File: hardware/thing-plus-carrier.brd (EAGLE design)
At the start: 160 x 100 mm, 6 parts, among them J1 THING_PLUS, U1 OKI-78SR-5/1.5-W36H-C

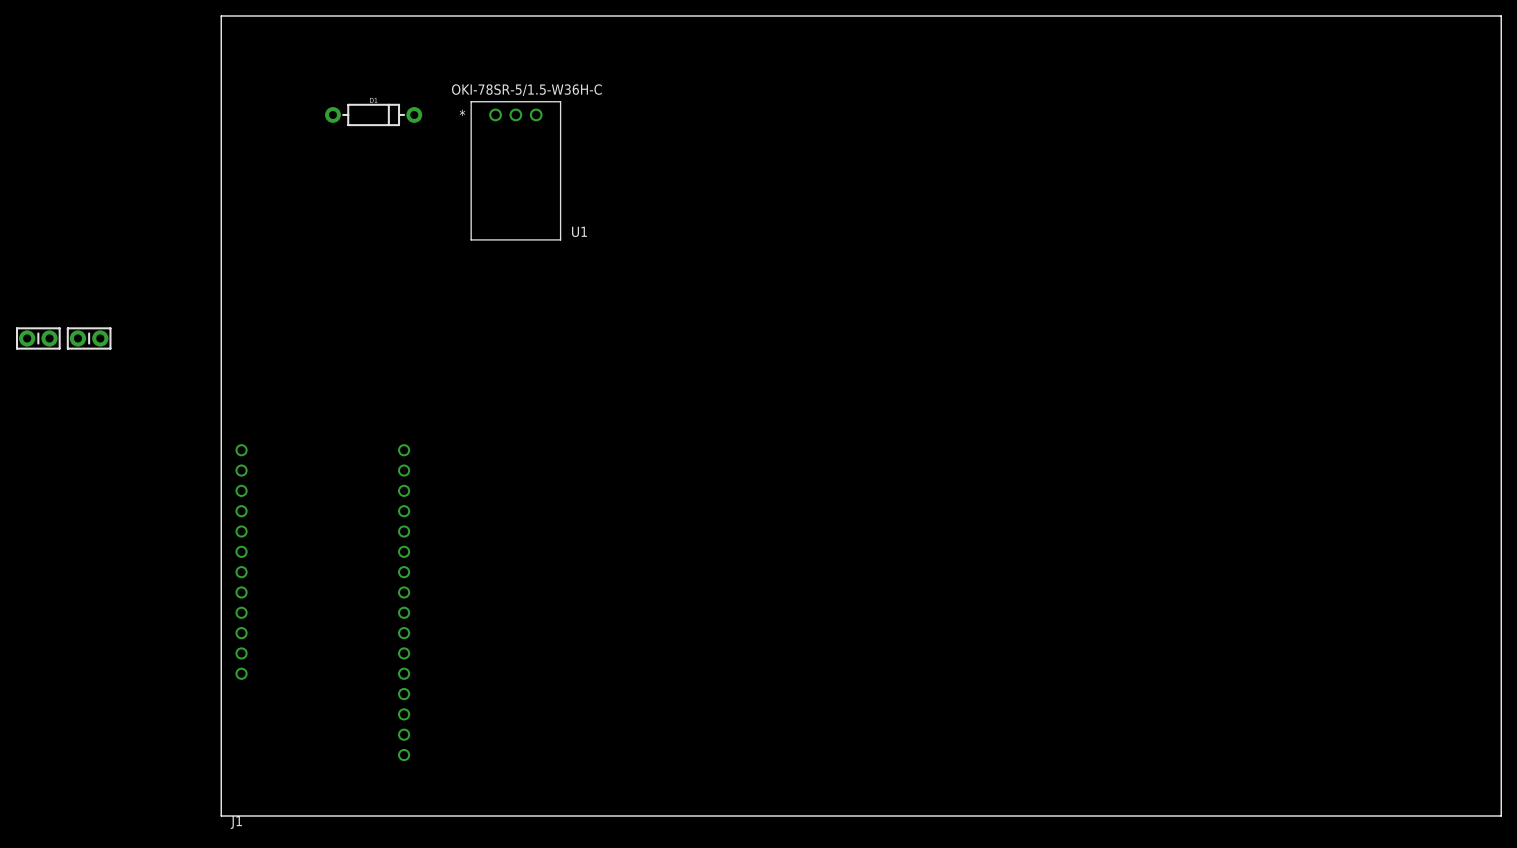
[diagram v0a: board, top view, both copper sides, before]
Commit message: laying out featherwing schematic
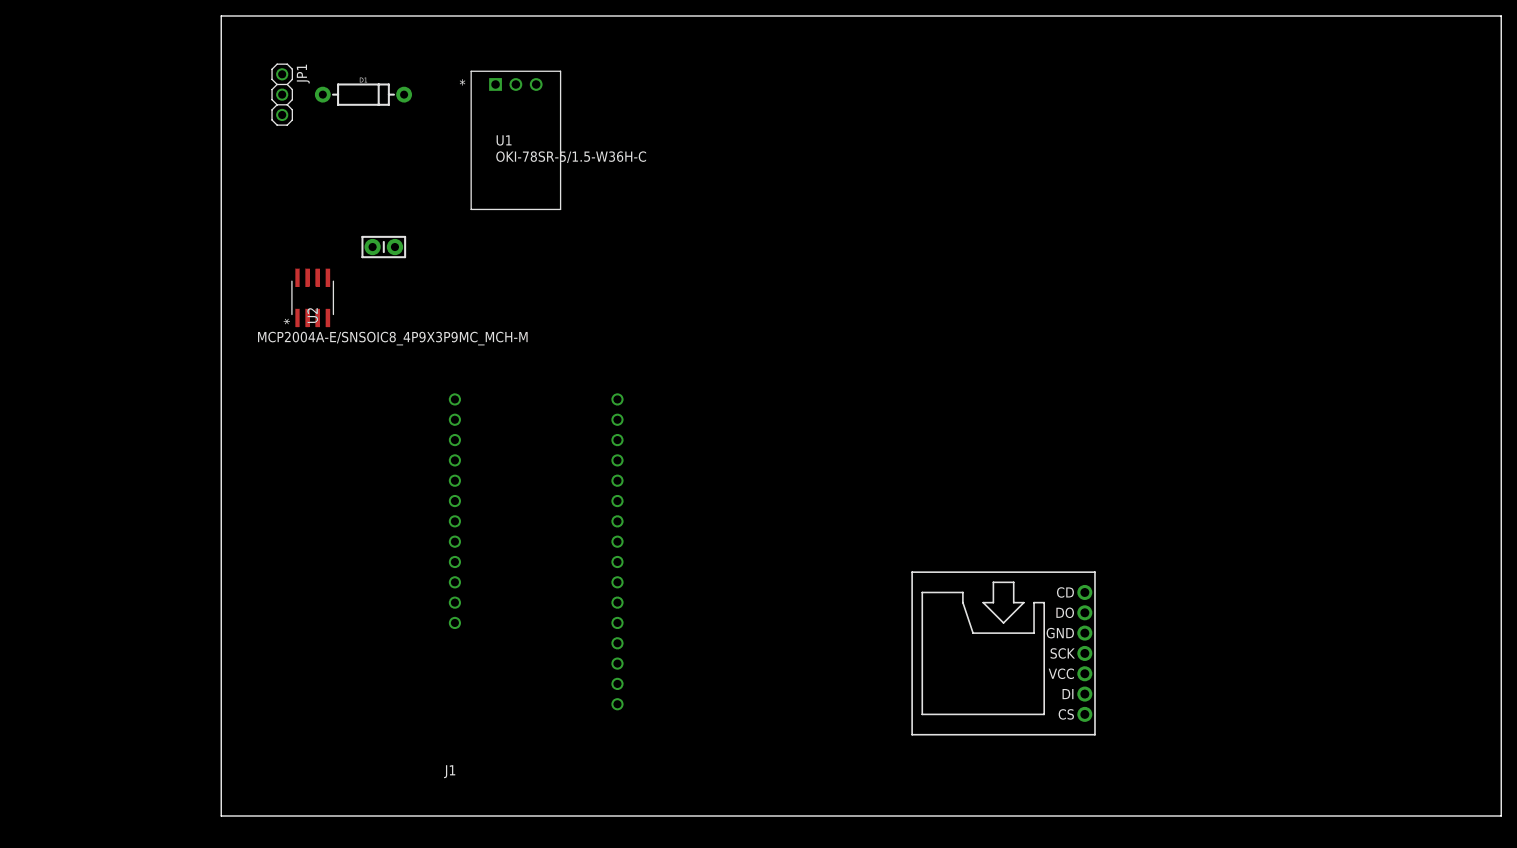
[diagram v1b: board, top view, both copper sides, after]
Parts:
- removed C2: 0.1uF, SparkFun-Capacitors:CAP-PTH-SMALL-KIT
- added JP1: (no value), adafruit:1X03
- added U2: MCP2004A-E/SNSOIC8_4P9X3P9MC_MCH-M, kbus-feather-carrier-bom:SOIC8_4P9X3P9MC_MCH-M
- added U3: MICROSD-BREAKOUT, SparkFun-Boards:MICROSD-BREAKOUT
- moved C1 38.6 mm to (20.3, 71.1)
- moved J1 27.4 mm to (39.4, 33.0)
- moved FRAME1 14.2 mm to (-12.7, 3.81)
- moved U1 3.81 mm to (34.3, 91.4)
- moved D1 2.84 mm to (17.8, 90.2)
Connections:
- removed net 0: J1.25, U1.2
- removed net N$1: D1.C, U1.1
- new net 12V: D1.C, U1.1, U2.7
- new net 3V3: J1.27, U3.VCC
- new net CD: U3.CD
- new net CIPO: U3.DO
- new net COPI: U3.DI
- new net FAULT: J1.7, U2.3
- new net GND: C1.2, J1.25, J1.26, JP1.1, U1.2, U2.5, U3.GND
- new net K-BUS: C1.1, JP1.3, U2.6
- new net RX: J1.15, U2.1
- new net SCK: U3.SCK
- new net SD-CS: U3.CS
- new net TRX-CS: J1.3, U2.2
- new net TX: J1.14, U2.4
- new net VBAT: D1.A, JP1.2

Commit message: Finished rev.1 board []~(￣▽￣)~* ; Updated docs
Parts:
- removed J1: THING_PLUS, SparkFun-Boards:THING_PLUS
- removed U1: OKI-78SR-5/1.5-W36H-C, kbus-feather-carrier-bom:OKI-78SR-5/1.5-W36H-C_MUR
- removed U2: MCP2004A-E/SNSOIC8_4P9X3P9MC_MCH-M, kbus-feather-carrier-bom:SOIC8_4P9X3P9MC_MCH-M
- added C2: 22uF, adafruit:C1206K
- added ESP32-THING-PLUS: THING_PLUS, SparkFun-Boards:THING_PLUS
- added LED1, LED2, LED3, LED4: (no value), adafruit:CHIPLED_0805
- added MCP2004A: MCP2004A-E/SNSOIC8_4P9X3P9MC_MCH-M, kbus-feather-carrier-bom:SOIC8_4P9X3P9MC_MCH-M
- added OKI-78SR: OKI-78SR-5/1.5-W36H-C, kbus-feather-carrier-bom:OKI-78SR-5/1.5-W36H-C_MUR
- added R1, R2, R3, R4: 1k, adafruit:R0805
- JP1: device adafruit:1X03 -> kbus-feather-carrier-bom:1X03
- U3: device SparkFun-Boards:MICROSD-BREAKOUT -> kbus-feather-carrier-bom:MICROSD-BREAKOUT
- moved U3 84.0 mm to (11.4, 24.1), turned to 90 degrees
- moved D1 31.8 mm to (17.8, 58.4)
- moved JP1 31.8 mm to (7.62, 58.4)
- moved C1 19.8 mm to (35.6, 58.4), turned to 90 degrees
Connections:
- new net N$1: ESP32-THING-PLUS.19, R3.1
- new net N$2: ESP32-THING-PLUS.24, R1.1
- new net N$3: ESP32-THING-PLUS.21, R2.1
- new net N$4: ESP32-THING-PLUS.17, R4.1
- new net N$5: LED4.A, R4.2
- new net N$6: LED3.A, R3.2
- new net N$7: LED2.A, R2.2
- new net N$8: LED1.A, R1.2
- net 12V: now also C2.1, MCP2004A.7, OKI-78SR.1; no longer U1.1, U2.7
- net 3V3: now also ESP32-THING-PLUS.27; no longer J1.27
- net 5V: now also ESP32-THING-PLUS.10, OKI-78SR.3; no longer J1.10, U1.3
- net CD: now also ESP32-THING-PLUS.4
- net CIPO: now also ESP32-THING-PLUS.8
- net COPI: now also ESP32-THING-PLUS.9
- net FAULT: now also ESP32-THING-PLUS.7, MCP2004A.3; no longer J1.7, U2.3
- net GND: now also C2.2, ESP32-THING-PLUS.25, ESP32-THING-PLUS.26, LED1.C, LED2.C, LED3.C, LED4.C, MCP2004A.5, OKI-78SR.2; no longer J1.25, J1.26, U1.2, U2.5
- net K-BUS: now also MCP2004A.6; no longer U2.6
- net RX: now also ESP32-THING-PLUS.15, MCP2004A.1; no longer J1.15, U2.1
- net SCK: now also ESP32-THING-PLUS.3
- net SD-CS: now also ESP32-THING-PLUS.5
- net TRX-CS: now also ESP32-THING-PLUS.13, MCP2004A.2; no longer J1.3, U2.2
- net TX: now also ESP32-THING-PLUS.14, MCP2004A.4; no longer J1.14, U2.4
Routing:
- net 3V3: track 0.00 -> 55.5 mm
- net FAULT: track 0.00 -> 52.0 mm, vias 0 -> 1
- net CIPO: track 0.00 -> 38.2 mm, vias 0 -> 1
- net 12V: track 0.00 -> 35.4 mm
- net K-BUS: track 0.00 -> 35.2 mm, vias 0 -> 1
- net CD: track 0.00 -> 33.9 mm, vias 0 -> 1
- net 5V: track 0.00 -> 33.2 mm
- net TX: track 0.00 -> 30.7 mm, vias 0 -> 1
- net RX: track 0.00 -> 26.5 mm, vias 0 -> 1
- net COPI: track 0.00 -> 25.2 mm
- net TRX-CS: track 0.00 -> 20.2 mm
- net SCK: track 0.00 -> 20.1 mm
- net GND: track 0.00 -> 17.6 mm, vias 0 -> 4
- net SD-CS: track 0.00 -> 13.2 mm
- net VBAT: track 0.00 -> 5.08 mm
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- added copper zone on layer 1, net GND
- added copper zone on layer 16, net GND
- added copper zone on layer 1, net N$9
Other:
- board size 160 x 100 mm -> 64.8 x 64.8 mm
- board text added: "Rev.03-2021"
- board text added: "github.com/jmederos"
- board text added: "kbus-featherwing"
